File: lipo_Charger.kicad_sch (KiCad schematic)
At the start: 98 parts, among them J1 Conn_01x02_Pin, J2 Conn_01x05, J3 Conn_01x04, J4 Conn_01x05, J5 Conn_01x04, Q1 NX7002AK_215(nch low power), Q2 NVTFS010N10MCLTAG(high power), Q3 NVTFS010N10MCLTAG(high power), Q4 NVTFS010N10MCLTAG(high power), Q5 NVTFS010N10MCLTAG(high power), Q6 NX7002AK_215(nch low power), Q7 NX7002AK_215(nch low power), Q8 NX7002AK_215(nch low power), U1 BQ25703ARSNR

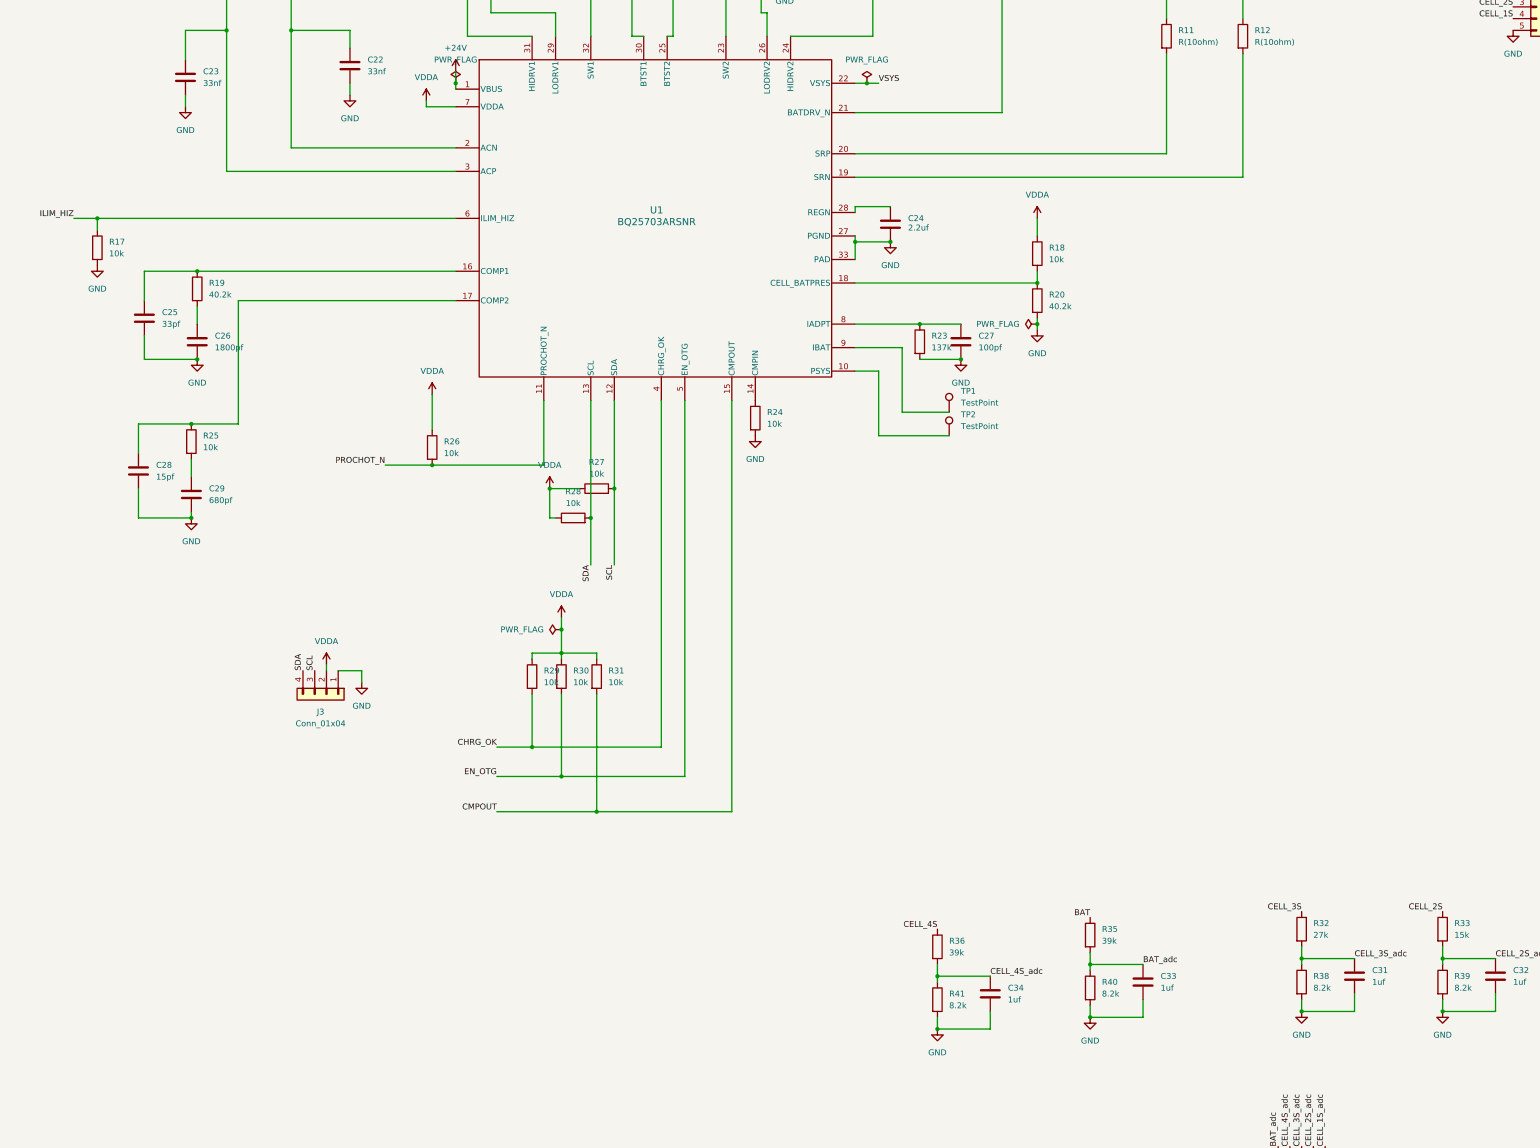
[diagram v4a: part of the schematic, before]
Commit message: need to seperate analog and digital ground and reroute everything
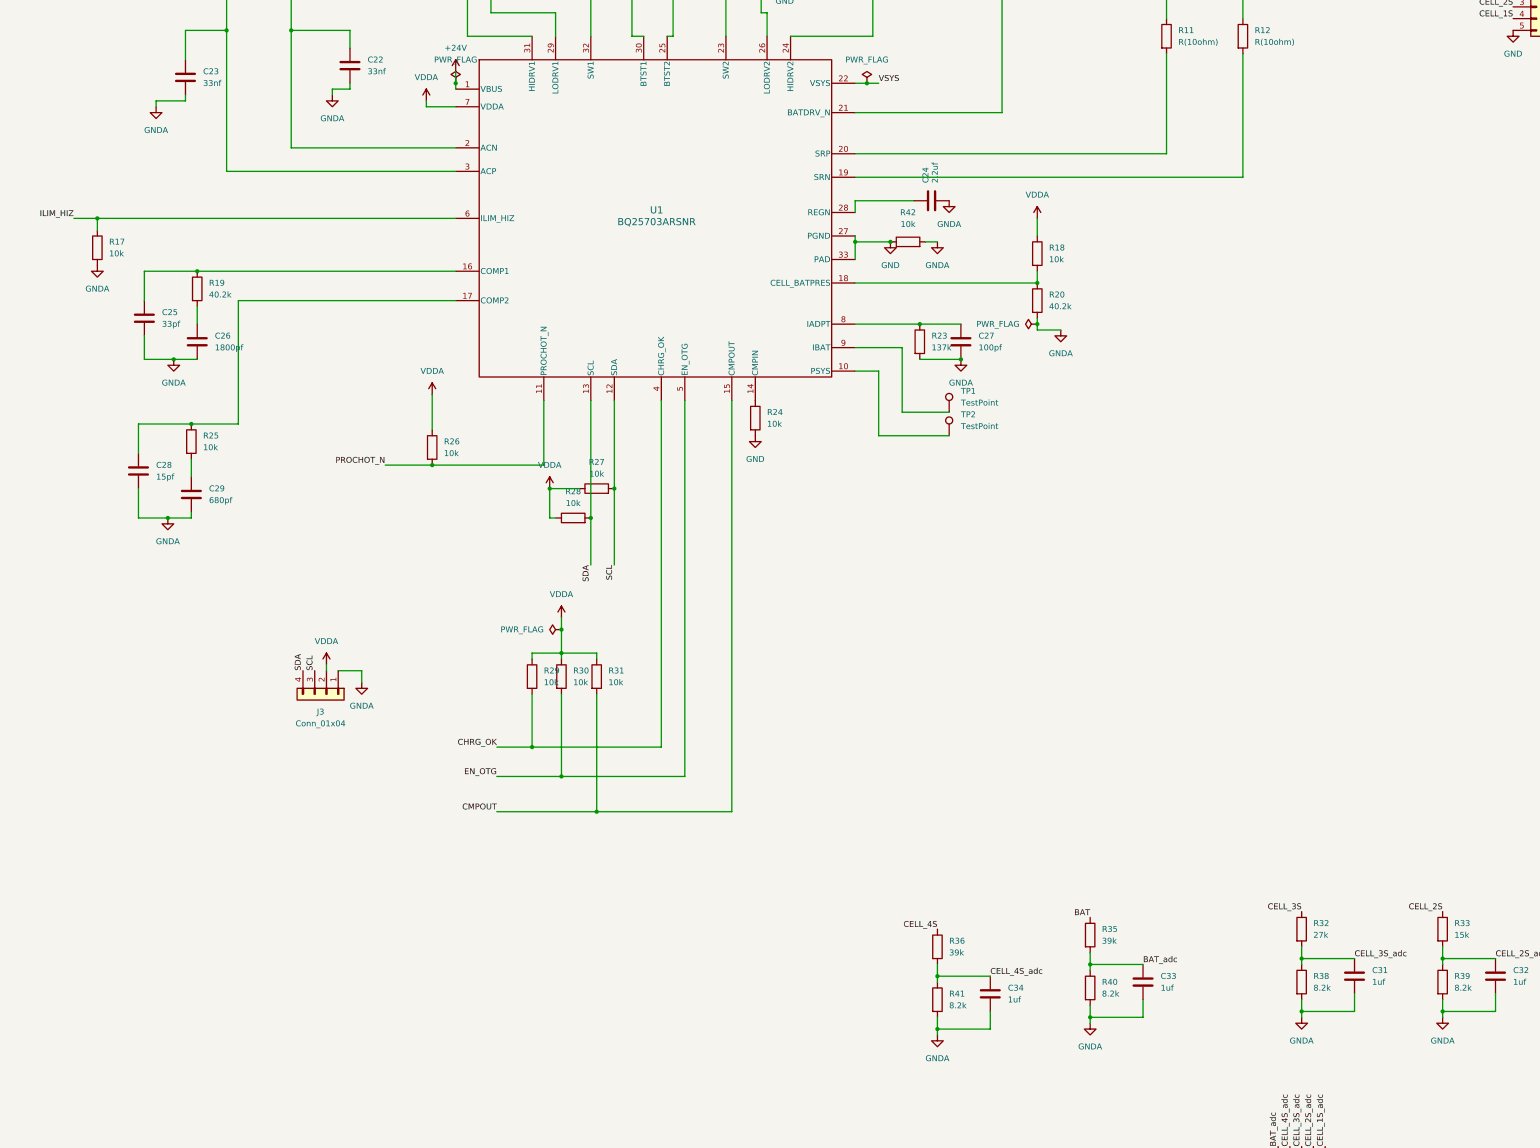
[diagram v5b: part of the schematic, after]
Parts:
- added R42: 10k, Inductor_SMD:L_0805_2012Metric_Pad1.05x1.20mm_HandSolder, symbol Lipo_charger_sym:R(10k)
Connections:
- net GND: now also R42.1; no longer C22.2, C23.2, C24.2, C25.2, C26.2, C27.2, C28.2, C29.2, C31.1, C32.1, C33.1, C34.1, J3.1 (Pin_1), R17.2, R20.2, R23.2, R38.2, R39.2, R40.2, R41.2
- new net GNDA: C22.2, C23.2, C24.2, C25.2, C26.2, C27.2, C28.2, C29.2, C31.1, C32.1, C33.1, C34.1, J3.1 (Pin_1), R17.2, R20.2, R23.2, R38.2, R39.2, R40.2, R41.2, R42.2
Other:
- moved on the sheet: C24

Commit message: all the links of the components has been assigned in the library for routing components placement is optimizes need routing
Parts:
- removed C24: 2.2uf, Diode_SMD:D_1206_3216Metric_Pad1.42x1.75mm_HandSolder, symbol Device:C
- removed C26: 1800pf, Capacitor_SMD:C_0805_2012Metric_Pad1.18x1.45mm_HandSolder, symbol Device:C
- removed J1: Conn_01x02_Pin, Connector_AMASS:AMASS_XT60-M_1x02_P7.20mm_Vertical, symbol Connector:Conn_01x02_Pin
- removed J2: Conn_01x05, Connector_JST:JST_XH_B5B-XH-A_1x05_P2.50mm_Vertical, symbol Connector_Generic:Conn_01x05
- removed J3: Conn_01x04, Connector_PinHeader_2.54mm:PinHeader_1x04_P2.54mm_Vertical, symbol Connector_Generic:Conn_01x04
- removed L1: 2.2uh, Inductor_SMD:L_10.4x10.4_H4.8, symbol Device:L
- removed R10, R14, R2, R22, R5: R, Resistor_SMD:R_2512_6332Metric_Pad1.40x3.35mm_HandSolder, symbol Device:R
- removed R38: 8.2k, Resistor_SMD:R_0603_1608Metric_Pad0.98x0.95mm_HandSolder, symbol Lipo_charger_sym:8.2k
- removed R4: R(10ohm), Resistor_SMD:R_0603_1608Metric_Pad0.98x0.95mm_HandSolder, symbol Lipo_charger_sym:R(10ohm)
- added C24: 2.2uf, Diode_SMD:D_1206_3216Metric_Pad1.42x1.75mm_HandSolder, symbol Lipo_charger_sym:2.2uf
- added C26: 1800pf, Diode_SMD:D_0805_2012Metric_Pad1.15x1.40mm_HandSolder, symbol Lipo_charger_sym:1800pf
- added J1: XT60PW-M, Lipo_Charger_footprint:AMASS_XT60PW-M, symbol Lipo_charger_sym:XT60PW-M
- added J3: balance_plug_4s, Connector_JST:JST_XH_B5B-XH-A_1x05_P2.50mm_Vertical, symbol Lipo_charger_sym:balance_plug_4s
- added J7: Conn_01x07, Connector_PinHeader_2.54mm:PinHeader_1x06_P2.54mm_Vertical, symbol Connector_Generic:Conn_01x07
- added L1: 2.2uh, Inductor_SMD:L_10.4x10.4_H4.8, symbol Lipo_charger_sym:2.2uh
- added R2: 8.2k, Resistor_SMD:R_0603_1608Metric_Pad0.98x0.95mm_HandSolder, symbol Lipo_charger_sym:8.2k
- added R4, R5: 0.01ohm, Resistor_SMD:R_2512_6332Metric_Pad1.40x3.35mm_HandSolder, symbol Lipo_charger_sym:0.01ohm
- added R43, R44, R45, R46: 47ohm, Resistor_SMD:R_2512_6332Metric_Pad1.40x3.35mm_HandSolder, symbol Lipo_charger_sym:47ohm
- C1, C10, C11, C12, C13, C14, C15, C16, C17, C2, C3, C4, C5, C6, C7, C8, C9: LCSC Part # (none) -> https://robu.in/product/10uf-10000nf-50v-capacitor-0805-smd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; LSCS Part # (none) -> https://robu.in/product/10uf-10000nf-50v-capacitor-0805-smd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
- C18, C30, C31, C32, C33, C34: LCSC Part # (none) -> https://robu.in/product/1uf-1000nf-50v-capacitor-0805-smd-p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
- C19, C21: LCSC Part # (none) -> https://robu.in/product/47nf-50v-capacitor-0603-smd-package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; LSCS Part # (none) -> https://robu.in/product/47nf-50v-capacitor-0603-smd-package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
- C20: LCSC Part # (none) -> https://robu.in/product/0-1uf-capacitor-smdc-0603/; LSCS Part # (none) -> https://robu.in/product/0-1uf-capacitor-smdc-0603/
- C22, C23: LCSC Part # (none) -> https://robu.in/product/33nf-0805-surface-mount-multilayer-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
- C25: LCSC Part # (none) -> https://robu.in/product/33pf-0603-surface-mount-multilayer-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; LSCS Part # (none) -> https://robu.in/product/33pf-0603-surface-mount-multilayer-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
- C27: LCSC Part # (none) -> https://robu.in/product/100pf-0603-surface-mount-multilayer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
- C28: LCSC Part # (none) -> https://robu.in/product/gjm1555c1h150fb01d-murata-electroni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; LSCS Part # (none) -> https://robu.in/product/gjm1555c1h150fb01d-murata-electroni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
- C29: LCSC Part # (none) -> https://robu.in/product/680pf-0-68nf-50v-capacitor-0603-smd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; LSCS Part # (none) -> https://robu.in/product/680pf-0-68nf-50v-capacitor-0603-smd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
- MOSFET1, MOSFET2, MOSFET3, MOSFET4, MOSFET5: LCSC Part # (none) -> https://robu.in/product/dmp3013sfv-hxy-mosfet-30v-55a-1-p-c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
- Q1, Q6, Q7, Q8: LCSC Part # (none) -> https://robu.in/product/nx7002akar-nexperia-nx7002akar-powe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
- Q2, Q3, Q4, Q5: LCSC Part # (none) -> https://robu.in/product/nvtfs008n04c-hxy-mosfet-40v-60a-1-n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
- R1, R13, R15, R16, R17, R18, R21, R24, R25, R26, R27, R28, R29, R3, R30, R31, R42, R6, R9: LCSC Part # (none) -> https://roboticsdna.in/product/10k%cf%89-thick-film-smd-res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
- R11, R12: LCSC Part # (none) -> https://robu.in/product/rc0603fr-0710rl-yageo-smd-chip-resi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
- R19, R20: LCSC Part # (none) -> https://robu.in/product/ac0603fr-0740k2l-yageo-res-thick-fi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
- R23: LCSC Part # (none) -> https://robu.in/product/ac0402fr-07137kl-yageo-res-thick-fi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
- R32: LCSC Part # (none) -> https://robu.in/product/ac0603fr-0727kl-yageo-res-thick-fil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
- R33: LCSC Part # (none) -> https://robu.in/product/ac0603fr-0715kl-yageo-res-thick-fil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
- R34: LCSC Part # (none) -> https://robu.in/product/3-3k-ohm-1-4w-0603-surface-mount-ch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; LSCS Part # (none) -> https://robu.in/product/3-3k-ohm-1-4w-0603-surface-mount-ch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
- R35, R36: LCSC Part # (none) -> https://robu.in/product/ac0603fr-0739kl-yageo-res-thick-fil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
- R37, R39, R40, R41: LCSC Part # (none) -> https://robu.in/product/rc0603fr-078k2l-yageo-res-thick-fil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; LSCS Part # (none) -> https://robu.in/product/rc0603fr-078k2l-yageo-res-thick-fil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
- R7, R8: LCSC Part # (none) -> https://robu.in/product/rc0805fr-074r99l-yageo-smd-chip-res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
- U1: LCSC Part # (none) -> https://robu.in/product/bq25713rsnr-texas-instruments-3-5v2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; LSCS Part # (none) -> https://robu.in/product/bq25713rsnr-texas-instruments-3-5v2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
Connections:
- net +24V: now also R5.1
- net BAT: now also J1.1 (P), R4.2
- net CELL_1S: now also J3.4 (Pin_4), R45.2
- net CELL_2S: now also J3.3 (Pin_3), R44.2
- net CELL_3S: now also J3.2 (Pin_2), R43.2
- net CELL_3S_adc: now also R2.1
- net CELL_4S: now also J3.1 (Pin_1)
- net CHRG_OK: now also J7.3 (Pin_3)
- net CMPOUT: now also J7.1 (Pin_1)
- net EN_OTG: now also J7.4 (Pin_4)
- net GND: now also J1.2 (N), J1.SH1 (SHIELD), J1.SH2 (SHIELD), J3.5 (Pin_5), R46.2; no longer R24.2
- net GNDA: now also R24.2, C24.2, C26.2, R2.2
- net ILIM_HIZ: now also J7.2 (Pin_2)
- net PROCHOT_N: now also J7.5 (Pin_5)
- net SCL: now also J7.7 (Pin_7)
- net SDA: now also J7.6 (Pin_6)
- net VSYS: now also R4.1
- net copper_pour1: now also R5.2
- net copper_pour2: now also L1.2
- net at MOSFET5.5 (D), MOSFET5.6 (D), MOSFET5.7 (D)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: now also R46.1
- net at R19.2: now also C26.1
- net at U1.28 (REGN): now also C24.1
- net at C19.1, Q2.1-2-3, Q4.5-6-7-8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: now also L1.1
- net at MOSFET4.5 (D), MOSFET4.6 (D), MOSFET4.7 (D)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: now also R45.1
- net at MOSFET1.5 (D), MOSFET1.6 (D), MOSFET1.7 (D)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: now also R43.1
- net at MOSFET3.5 (D), MOSFET3.6 (D), MOSFET3.7 (D)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: now also R44.1
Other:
- note removed: "check the footprint of inductor"

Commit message: power side routing is done need to look into where i switch layers balancing side and interection with stm has to be done
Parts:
- removed R42: 10k, Inductor_SMD:L_0805_2012Metric_Pad1.05x1.20mm_HandSolder, symbol Lipo_charger_sym:R(10k)
- C26: LCSC Part # https://robu.in/product/cdrh104r-2-2%CE%BCh-power-inductor-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 -> https://robu.in/product/1-8nf-1800pf-50v-capacitor-0805-smd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
- J7: footprint Connector_PinHeader_2.54mm:PinHeader_1x06_P2.54mm_Vertical -> Connector_PinHeader_2.54mm:PinHeader_1x07_P2.54mm_Vertical
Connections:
- net CHRG_OK: now also J7.5 (Pin_5); no longer J7.3 (Pin_3)
- net CMPOUT: now also J7.7 (Pin_7); no longer J7.1 (Pin_1)
- net ILIM_HIZ: now also J7.3 (Pin_3); no longer J7.2 (Pin_2)
- net PROCHOT_N: now also J7.6 (Pin_6); no longer J7.5 (Pin_5)
- net SCL: now also J7.2 (Pin_2); no longer J7.7 (Pin_7)
- net SDA: now also J7.1 (Pin_1); no longer J7.6 (Pin_6)
- net copper_pour2: now also C19.1, L1.1, Q2.1-2-3, Q4.5-6-7-8, U1.32 (SW1); no longer C21.1, L1.2, Q3.1-2-3, Q5.5-6-7-8, U1.23 (SW2)
- net copper_pour3: now also C21.1, L1.2, Q3.1-2-3, Q5.5-6-7-8, U1.23 (SW2); no longer MOSFET2.5 (D), MOSFET2.6 (D), MOSFET2.7 (D), MOSFET2.8 (D), Q3.5-6-7-8
- new net: MOSFET2.5 (D), MOSFET2.6 (D), MOSFET2.7 (D), MOSFET2.8 (D), Q3.5-6-7-8
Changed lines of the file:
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@@
 	(generator_version "9.0")
 	(paper "A3")
+	(rectangle
+		(start 233.68 163.83)
+		(end 255.27 177.8)
+		(stroke
+			(width 0)
+			(type default)
+		)
+		(fill
+			(type none)
+		)
+	)
 	(junction
 		(at 49.53 35.56)
@@
 	)
 	(junction
-		(at 240.03 168.91)
-		(diameter 0)
-		(color 0 0 0 0)
-	)
-	(junction
 		(at 96.52 123.19)
 		(diameter 0)
@@
 	)
 	(label "SDA"
-		(at 60.96 264.16 90)
+		(at 73.66 264.16 90)
 		(effects
 			(font
@@
 	)
 	(label "copper_pour3"
-		(at 251.46 90.17 0)
+		(at 218.44 90.17 0)
 		(effects
 			(font
@@
 	)
 	(label "ILIM_HIZ"
-		(at 71.12 264.16 90)
+		(at 68.58 264.16 90)
 		(effects
 			(font
@@
 	)
 	(label "PROCHOT_N"
-		(at 63.5 264.16 90)
+		(at 60.96 264.16 90)
 		(effects
 			(font
@@
 	)
 	(label "copper_pour2"
-		(at 218.44 90.17 0)
+		(at 170.18 90.17 0)
 		(effects
 			(font
@@
 	)
 	(label "CHRG_OK"
-		(at 68.58 264.16 90)
+		(at 63.5 264.16 90)
 		(effects
 			(font
@@
 	)
 	(label "SCL"
-		(at 58.42 264.16 90)
+		(at 71.12 264.16 90)
 		(effects
 			(font
@@
 	)
 	(label "CMPOUT"
-		(at 73.66 264.16 90)
+		(at 58.42 264.16 90)
 		(effects
 			(font
@@
 	)
 	(symbol
+		(lib_id "Lipo_charger_sym:1800pf")
+		(at 90.17 190.5 0)
+		(unit 1)
+		(exclude_from_sim no)
+		(in_bom yes)
+		(on_board yes)
+		(dnp no)
+		(fields_autoplaced yes)
+		(property "Reference" "C26"
+			(at 93.98 189.2299 0)
+			(effects
+				(font
+					(size 1.27 1.27)
+				)
+				(justify left)
+			)
+		)
+		(property "Value" "1800pf"
+			(at 93.98 191.7699 0)
+			(effects
+				(font
+					(size 1.27 1.27)
+				)
+				(justify left)
+			)
+		)
+		(property "Footprint" "Diode_SMD:D_0805_2012Metric_Pad1.15x1.40mm_HandSolder"
+			(at 91.1352 194.31 0)
+			(effects
+				(font
+					(size 1.27 1.27)
+				)
+				(hide yes)
+			)
+		)
+		(property "Datasheet" "~"
+			(at 90.17 190.5 0)
+			(effects
+				(font
+					(size 1.27 1.27)
+				)
+				(hide yes)
+			)
+		)
+		(property "Description" "Unpolarized capacitor"
+			(at 90.17 190.5 0)
+			(effects
+				(font
+					(size 1.27 1.27)
+				)
+				(hide yes)
+			)
+		)
+		(property "LCSC Part #" "https://robu.in/product/1-8nf-1800pf-50v-capacitor-0805-smd-package-pack-of-30/"
+			(at 90.17 190.5 0)
+			(effects
+				(font
+					(size 1.27 1.27)
+				)
+				(hide yes)
+			)
+		)
+		(pin "2"
+		)
+		(pin "1"
+		)
+		(instances
+			(project ""
+				(path "/4a18423b-6328-407d-a1e3-fa6705870417"
+					(reference "C26")
+					(unit 1)
+				)
+			)
+		)
+	)
+	(symbol
 		(lib_id "Lipo_charger_sym:C 10uf")
 		(at 85.09 31.75 0)
@@
 	(symbol
 		(lib_id "Lipo_charger_sym:R(10k)")
-		(at 243.84 168.91 90)
-		(unit 1)
-		(exclude_from_sim no)
-		(in_bom yes)
-		(on_board yes)
-		(dnp no)
-		(fields_autoplaced yes)
-		(property "Reference" "R42"
-			(at 243.84 162.56 90)
-			(effects
-				(font
-					(size 1.27 1.27)
-				)
-			)
-		)
-		(property "Value" "10k"
-			(at 243.84 165.1 90)
-			(effects
-				(font
-					(size 1.27 1.27)
-				)
-			)
-		)
-		(property "Footprint" "Inductor_SMD:L_0805_2012Metric_Pad1.05x1.20mm_HandSolder"
-			(at 243.84 170.688 90)
-			(effects
-				(font
-					(size 1.27 1.27)
-				)
-				(hide yes)
-			)
-		)
-		(property "Datasheet" "~"
-			(at 243.84 168.91 0)
-			(effects
-				(font
-					(size 1.27 1.27)
-				)
-				(hide yes)
-			)
-		)
-		(property "Description" "Resistor"
-			(at 243.84 168.91 0)
-			(effects
-				(font
-					(size 1.27 1.27)
-				)
-				(hide yes)
-			)
-		)
-		(property "link" "https://roboticsdna.in/product/10k%cf%89-thick-film-smd-resistor-0805-%c2%b15-tolerence-100-pcs/"
-			(at 243.84 168.91 0)
-			(effects
-				(font
-					(size 1.27 1.27)
-				)
-				(hide yes)
-			)
-		)
-		(property "LCSC Part #" "https://roboticsdna.in/product/10k%cf%89-thick-film-smd-resistor-0805-%c2%b15-tolerence-100-pcs/"
-			(at 243.84 168.91 0)
-			(effects
-				(font
-					(size 1.27 1.27)
-				)
-				(hide yes)
-			)
-		)
-		(pin "1"
-		)
-		(pin "2"
-		)
-		(instances
-			(project "lipo_Charger"
-				(path "/4a18423b-6328-407d-a1e3-fa6705870417"
-					(reference "R42")
-					(unit 1)
-				)
-			)
-		)
-	)
-	(symbol
-		(lib_id "Lipo_charger_sym:R(10k)")
 		(at 176.53 262.89 0)
 		(unit 1)
@@
 	)
 	(symbol
-		(lib_id "Lipo_charger_sym:1800pf")
-		(at 90.17 190.5 0)
-		(unit 1)
-		(exclude_from_sim no)
-		(in_bom yes)
-		(on_board yes)
-		(dnp no)
-		(fields_autoplaced yes)
-		(property "Reference" "C26"
-			(at 93.98 189.2299 0)
-			(effects
-				(font
-					(size 1.27 1.27)
-				)
-				(justify left)
-			)
-		)
-		(property "Value" "1800pf"
-			(at 93.98 191.7699 0)
-			(effects
-				(font
-					(size 1.27 1.27)
-				)
-				(justify left)
-			)
-		)
-		(property "Footprint" "Diode_SMD:D_0805_2012Metric_Pad1.15x1.40mm_HandSolder"
-			(at 91.1352 194.31 0)
-			(effects
-				(font
-					(size 1.27 1.27)
-				)
-				(hide yes)
-			)
-		)
-		(property "Datasheet" "~"
-			(at 90.17 190.5 0)
-			(effects
-				(font
-					(size 1.27 1.27)
-				)
-				(hide yes)
-			)
-		)
-		(property "Description" "Unpolarized capacitor"
-			(at 90.17 190.5 0)
-			(effects
-				(font
-					(size 1.27 1.27)
-				)
-				(hide yes)
-			)
-		)
-		(property "LCSC Part #" "https://robu.in/product/cdrh104r-2-2%CE%BCh-power-inductor-pack-of-5/?gad_source=1&gad_campaignid=17427802703&gbraid=0AAAAADvLFWeYd6KQJmaof5AqwX7G6G7RK&gclid=CjwKCAjw687NBhB4EiwAQ645dmHAlDrRVuziQAJbPZqMJFAUlKgMQ-ZthCMAKLuhHOvZczBMktniURoCJv0QAvD_BwE#tab-robu_other_tab"
-			(at 90.17 190.5 0)
-			(effects
-				(font
-					(size 1.27 1.27)
-				)
-				(hide yes)
-			)
-		)
-		(pin "1"
-		)
-		(pin "2"
-		)
-		(instances
-			(project ""
-				(path "/4a18423b-6328-407d-a1e3-fa6705870417"
-					(reference "C26")
-					(unit 1)
-				)
-			)
-		)
-	)
-	(symbol
 		(lib_id "Lipo_charger_sym:balance_plug_4s")
 		(at 379.73 118.11 0)
@@
 			)
 		)
-		(property "Footprint" "Connector_PinHeader_2.54mm:PinHeader_1x06_P2.54mm_Vertical"
+		(property "Footprint" "Connector_PinHeader_2.54mm:PinHeader_1x07_P2.54mm_Vertical"
 			(at 66.04 269.24 0)
 			(effects

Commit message: done everything need to check before ordering once
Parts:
- added D1, D2, D3, D4: LED, LED_THT:LED_D5.0mm, symbol Device:LED
- added J2, J6: Conn_01x01, Connector_PinHeader_2.54mm:PinHeader_1x01_P2.54mm_Vertical, symbol Connector_Generic:Conn_01x01
- added J8: Conn_01x04, Connector_PinHeader_2.54mm:PinHeader_1x04_P2.54mm_Vertical, symbol Connector_Generic:Conn_01x04
- added R10: 0ohm, Resistor_SMD:R_0603_1608Metric_Pad0.98x0.95mm_HandSolder, symbol Lipo_charger_sym:0ohm
- added R14, R22, R38, R42: R, Resistor_THT:R_Axial_DIN0204_L3.6mm_D1.6mm_P5.08mm_Horizontal, symbol Device:R
- added TP4: TestPoint, TestPoint:TestPoint_THTPad_4.0x4.0mm_Drill2.0mm, symbol Connector:TestPoint
- TP3: footprint TestPoint:TestPoint_Pad_4.0x4.0mm -> TestPoint:TestPoint_THTPad_4.0x4.0mm_Drill2.0mm
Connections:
- net GND: now also C24.2, D1.1 (K), D2.1 (K), D3.1 (K), D4.1 (K), R10.1, TP4.1; no longer C30.1, R37.2
- net GNDA: now also C30.1, R37.2, J6.1 (Pin_1), R10.2; no longer C24.2
- net VDDA: now also J2.1 (Pin_1)
- new net: MOSFET2.5 (D), Q3.5-6-7-8
- new net: MOSFET4.5 (D), R45.1
- new net: J8.2 (Pin_2), R22.1
- new net: D2.2 (A), R22.2
- new net: D3.2 (A), R38.2
- new net: MOSFET3.5 (D), R44.1
- new net: J8.1 (Pin_1), R14.1
- new net: J8.3 (Pin_3), R38.1
- new net: J8.4 (Pin_4), R42.1
- new net: D4.2 (A), R42.2
- new net: MOSFET5.5 (D), R46.1
- new net: D1.2 (A), R14.2
- new net: MOSFET1.5 (D), R43.1
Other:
- moved on the sheet: C1, C10, C11, C12, C13, C14, C15, C16, C17, C18, C19, C2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
